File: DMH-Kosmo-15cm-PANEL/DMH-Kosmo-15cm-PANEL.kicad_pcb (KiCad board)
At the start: 2 copper layers, 100 x 200 mm, 4 parts

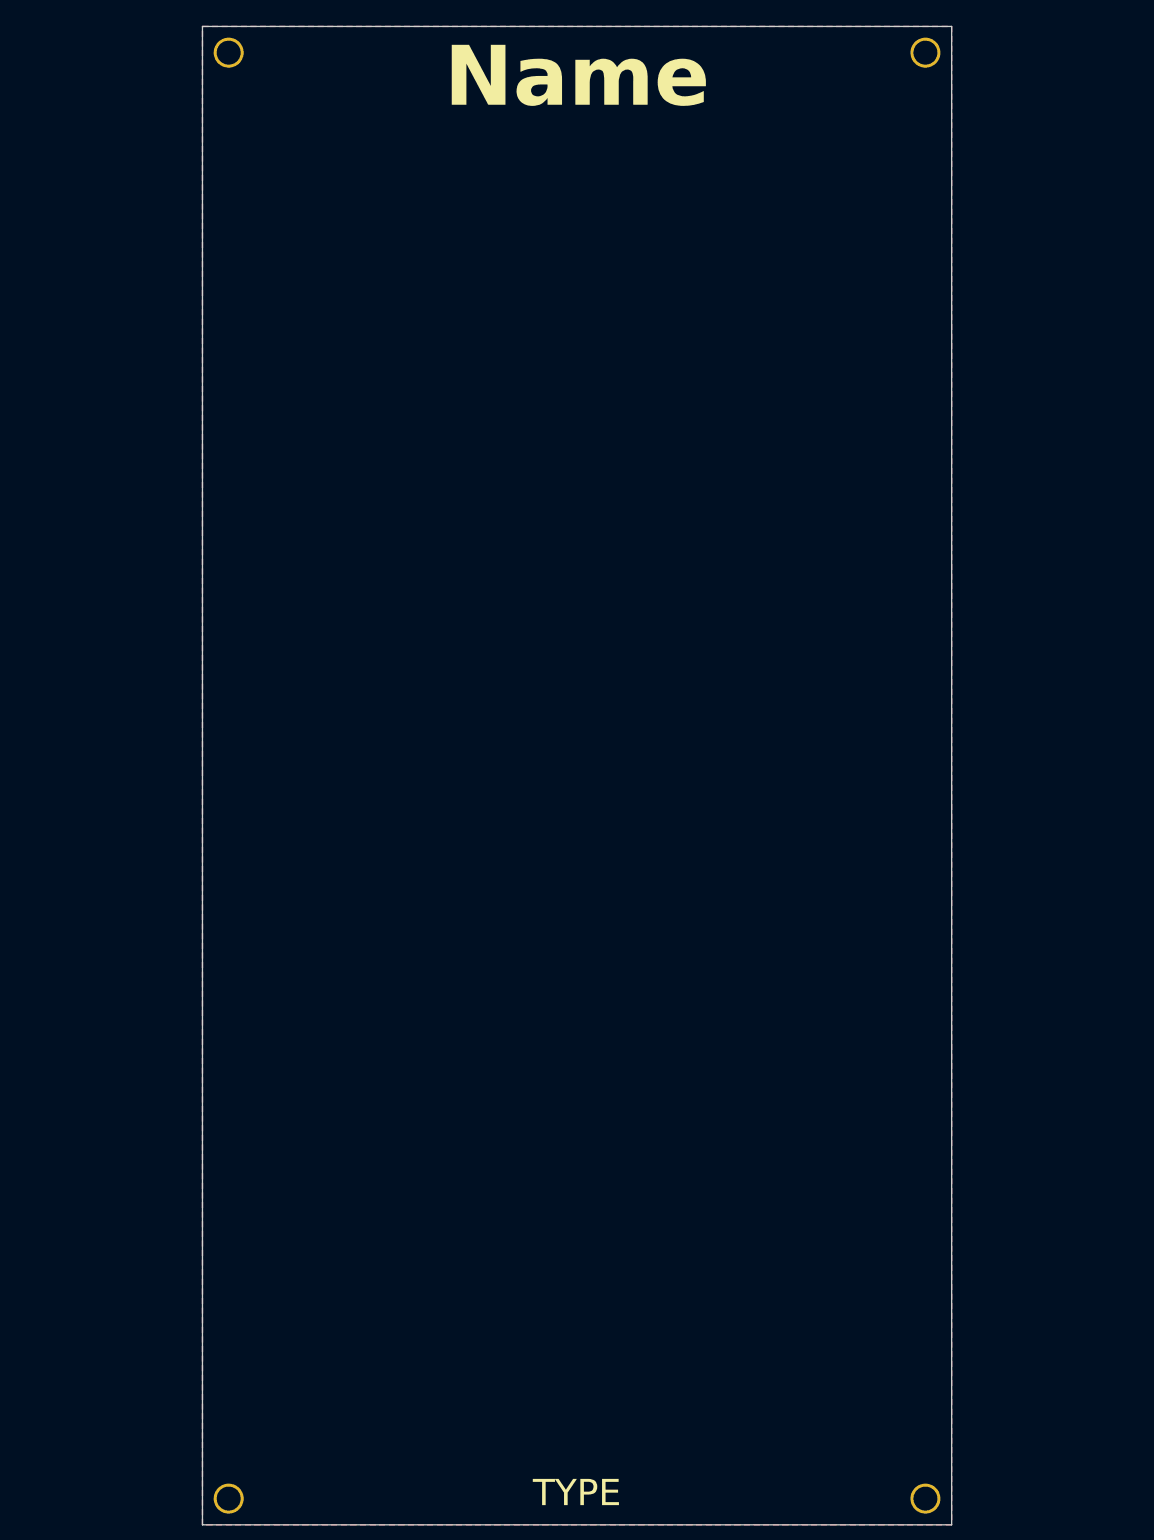
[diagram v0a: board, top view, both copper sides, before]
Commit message: Added 15cm templates
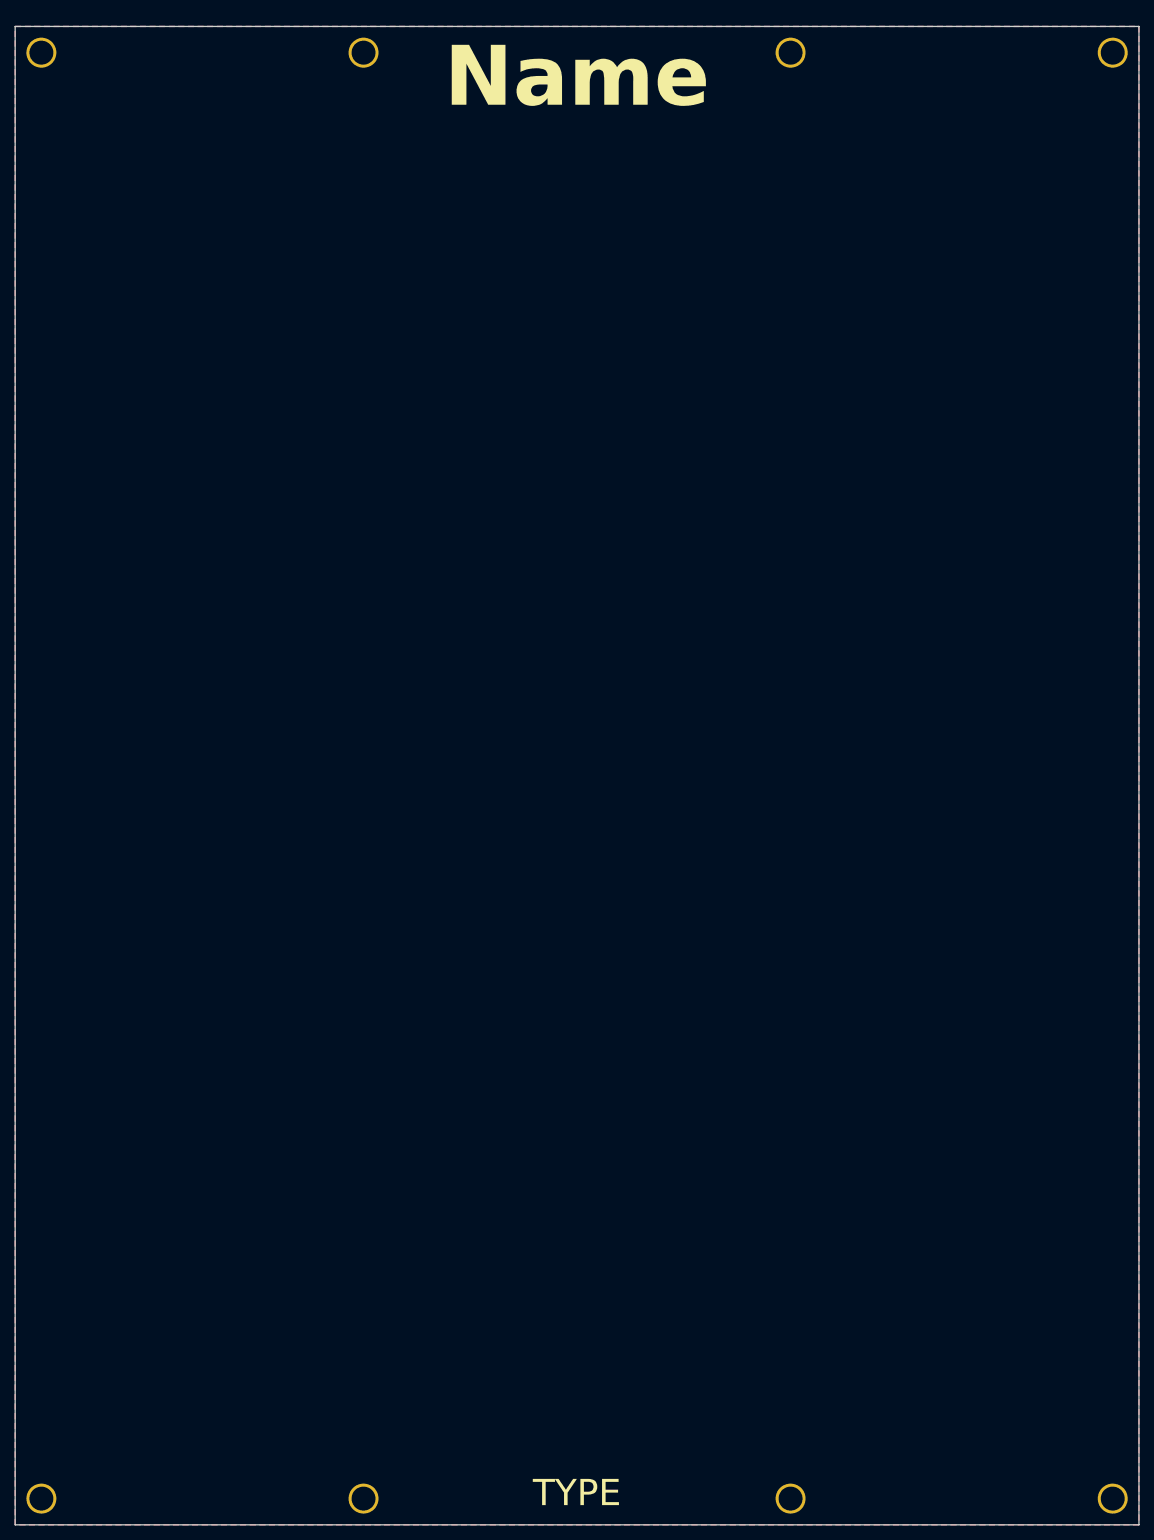
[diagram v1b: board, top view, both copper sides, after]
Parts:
- added H51: MountingHole_Rails, SynthStuff:MountingHole_Rails, F.Cu at (71.5, 33.5)
- added H52: MountingHole_Rails, SynthStuff:MountingHole_Rails, F.Cu at (128.5, 33.5)
- added H53: MountingHole_Rails, SynthStuff:MountingHole_Rails, F.Cu at (71.5, 226.5)
- added H54: MountingHole_Rails, SynthStuff:MountingHole_Rails, F.Cu at (128.5, 226.5)
- moved H1 25.0 mm to (28.5, 33.5)
- moved H2 25.0 mm to (171.5, 33.5)
- moved H3 25.0 mm to (28.5, 226.5)
- moved H4 25.0 mm to (171.5, 226.5)
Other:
- board size 100 x 200 mm -> 150 x 200 mm
